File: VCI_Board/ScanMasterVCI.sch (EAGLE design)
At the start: 77 parts, among them IC1 XMEGA16A4A, Q13 MMBT3904, Q14 MMBT3904, Q15 MMBT3904, Q2 NDC7002N, Q3 MMBT3904, Q5 NTZD5110N, Q6 MMBT3904, Q7 ZXMP6A17G, Q8 MMBT4403, Q9 NDC7002N, U1 MAX17502FATB+, U2 SN65HVDA195-Q1, U3 MAX17502EATB+, U4 L78L08ABUTR

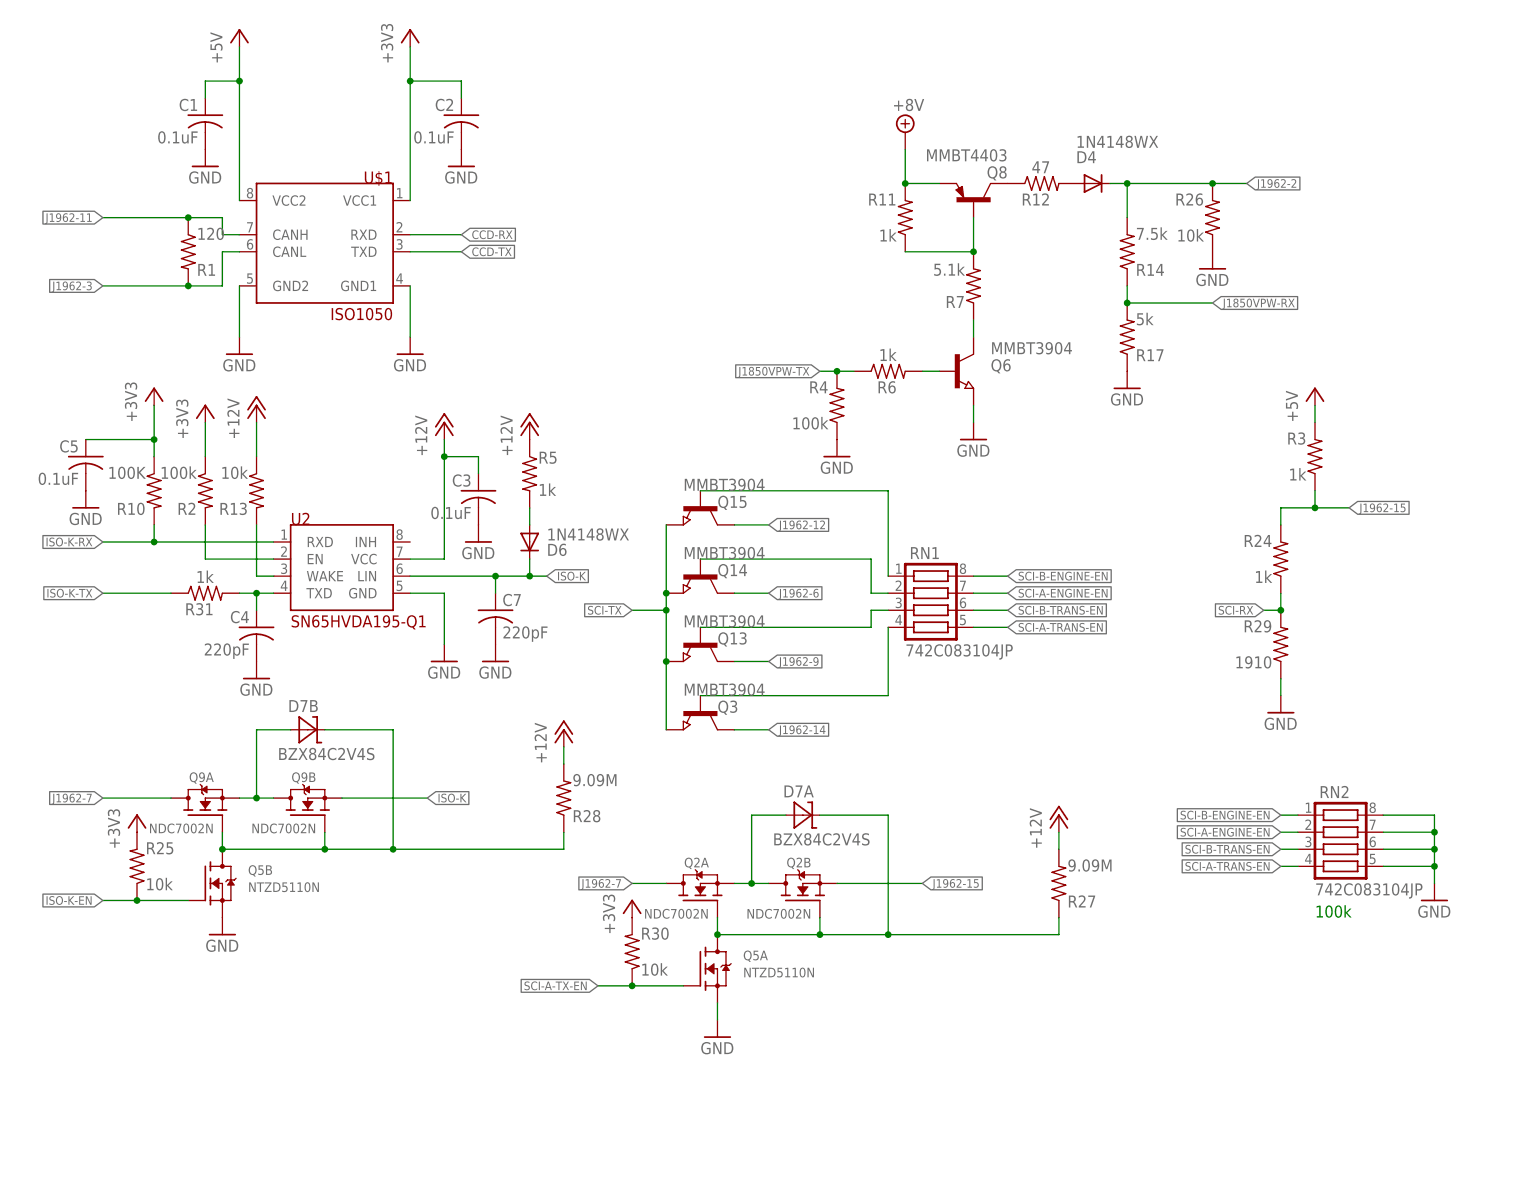
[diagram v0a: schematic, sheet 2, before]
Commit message: It was pointed out to me that the legs of my transistor were reversed. Fixed.
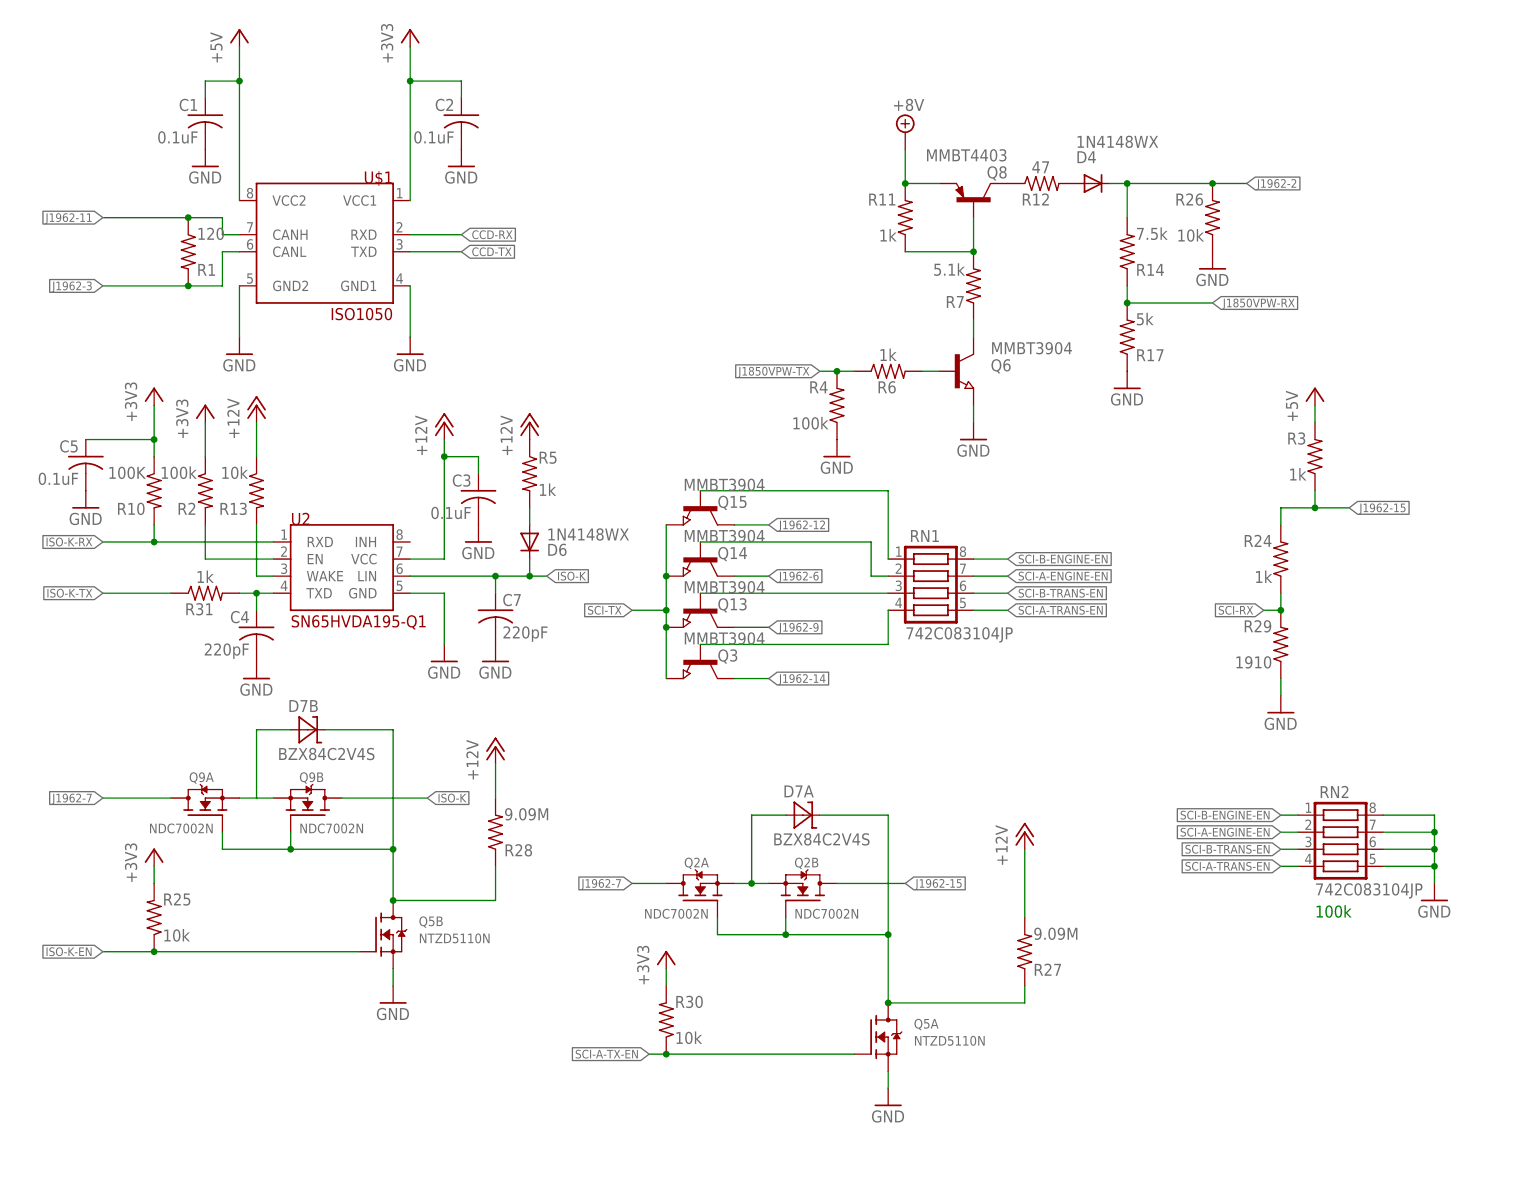
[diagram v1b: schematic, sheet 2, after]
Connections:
- net ISO-K: now also Q9B.D; no longer Q9B.S
- net J1962-15: now also Q2B.D; no longer Q2B.S
- net N$1: now also Q2B.S; no longer Q2B.D
- net N$4: now also Q9B.S; no longer Q9B.D
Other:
- moved on the sheet: Q13, Q14, Q3, Q5A, Q5B, R25, R27, R28, R30, RN1

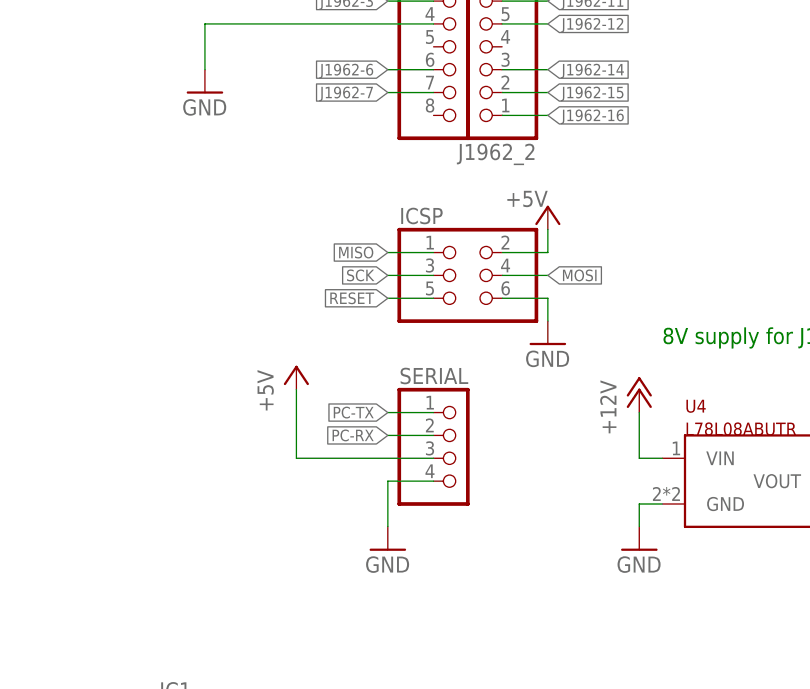
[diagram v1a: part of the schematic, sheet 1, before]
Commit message: Centered the OBD-II "header" pins on the board. Had to move a ton of stuff around to accomodate moving the OBD-II header to the center of the board, but I am now back to auto-router able to 100% route the board.
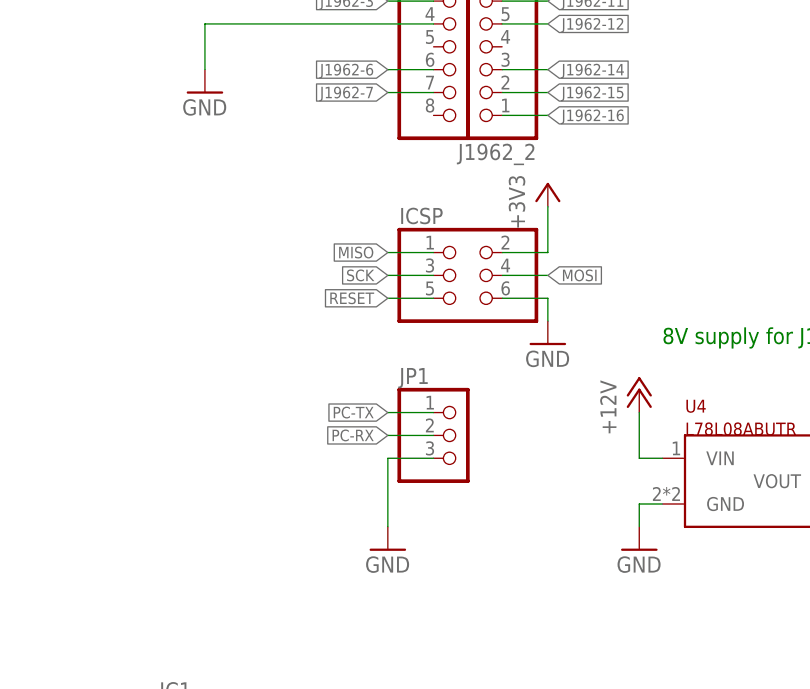
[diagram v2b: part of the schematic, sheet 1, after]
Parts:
- removed SERIAL: (no value), pinhead:PINHD-1X4
- added JP1: (no value), pinhead:PINHD-1X3
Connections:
- net +3V3: now also ICSP.2
- net +5V: no longer ICSP.2, SERIAL.3
- net GND: now also JP1.3; no longer SERIAL.4
- net PC-RX: now also JP1.2; no longer SERIAL.2
- net PC-TX: now also JP1.1; no longer SERIAL.1

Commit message: Started organizing the board. Keeping +12V components next to each other to try and reduce vias. Same for +5v and +3V3. So far not very successful, but it's a WIP.
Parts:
- C1: device adafruit:C-USC0805 -> adafruit:C-USC0603
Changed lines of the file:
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@@
 <grid distance="0.1" unitdist="inch" unit="inch" style="lines" multiple="1" display="no" altdistance="0.01" altunitdist="inch" altunit="inch"/>
 <layers>
-<layer number="1" name="Top" color="4" fill="1" visible="no" active="no"/>
-<layer number="16" name="Bottom" color="1" fill="1" visible="no" active="no"/>
-<layer number="17" name="Pads" color="2" fill="1" visible="no" active="no"/>
-<layer number="18" name="Vias" color="2" fill="1" visible="no" active="no"/>
-<layer number="19" name="Unrouted" color="6" fill="1" visible="no" active="no"/>
-<layer number="20" name="Dimension" color="24" fill="1" visible="no" active="no"/>
-<layer number="21" name="tPlace" color="7" fill="1" visible="no" active="no"/>
-<layer number="22" name="bPlace" color="7" fill="1" visible="no" active="no"/>
-<layer number="23" name="tOrigins" color="15" fill="1" visible="no" active="no"/>
-<layer number="24" name="bOrigins" color="15" fill="1" visible="no" active="no"/>
-<layer number="25" name="tNames" color="7" fill="1" visible="no" active="no"/>
-<layer number="26" name="bNames" color="7" fill="1" visible="no" active="no"/>
-<layer number="27" name="tValues" color="7" fill="1" visible="no" active="no"/>
-<layer number="28" name="bValues" color="7" fill="1" visible="no" active="no"/>
+<layer number="1" name="Top" color="4" fill="1" visible="yes" active="no"/>
+<layer number="16" name="Bottom" color="1" fill="1" visible="yes" active="no"/>
+<layer number="17" name="Pads" color="2" fill="1" visible="yes" active="no"/>
+<layer number="18" name="Vias" color="2" fill="1" visible="yes" active="no"/>
+<layer number="19" name="Unrouted" color="6" fill="1" visible="yes" active="no"/>
+<layer number="20" name="Dimension" color="24" fill="1" visible="yes" active="no"/>
+<layer number="21" name="tPlace" color="7" fill="1" visible="yes" active="no"/>
+<layer number="22" name="bPlace" color="7" fill="1" visible="yes" active="no"/>
+<layer number="23" name="tOrigins" color="15" fill="1" visible="yes" active="no"/>
+<layer number="24" name="bOrigins" color="15" fill="1" visible="yes" active="no"/>
+<layer number="25" name="tNames" color="7" fill="1" visible="yes" active="no"/>
+<layer number="26" name="bNames" color="7" fill="1" visible="yes" active="no"/>
+<layer number="27" name="tValues" color="7" fill="1" visible="yes" active="no"/>
+<layer number="28" name="bValues" color="7" fill="1" visible="yes" active="no"/>
 <layer number="29" name="tStop" color="7" fill="3" visible="no" active="no"/>
 <layer number="30" name="bStop" color="7" fill="6" visible="no" active="no"/>
@@
 <layer number="35" name="tGlue" color="7" fill="4" visible="no" active="no"/>
 <layer number="36" name="bGlue" color="7" fill="5" visible="no" active="no"/>
-<layer number="37" name="tTest" color="7" fill="1" visible="no" active="no"/>
-<layer number="38" name="bTest" color="7" fill="1" visible="no" active="no"/>
+<layer number="37" name="tTest" color="7" fill="1" visible="yes" active="no"/>
+<layer number="38" name="bTest" color="7" fill="1" visible="yes" active="no"/>
 <layer number="39" name="tKeepout" color="4" fill="11" visible="no" active="no"/>
 <layer number="40" name="bKeepout" color="1" fill="11" visible="no" active="no"/>
@@
 <layer number="44" name="Drills" color="7" fill="1" visible="no" active="no"/>
 <layer number="45" name="Holes" color="7" fill="1" visible="no" active="no"/>
-<layer number="46" name="Milling" color="3" fill="1" visible="no" active="no"/>
-<layer number="47" name="Measures" color="7" fill="1" visible="no" active="no"/>
-<layer number="48" name="Document" color="7" fill="1" visible="no" active="no"/>
-<layer number="49" name="Reference" color="7" fill="1" visible="no" active="no"/>
-<layer number="50" name="dxf" color="7" fill="1" visible="no" active="no"/>
-<layer number="51" name="tDocu" color="7" fill="1" visible="no" active="no"/>
-<layer number="52" name="bDocu" color="7" fill="1" visible="no" active="no"/>
-<layer number="53" name="tGND_GNDA" color="7" fill="9" visible="no" active="no"/>
-<layer number="54" name="bGND_GNDA" color="1" fill="9" visible="no" active="no"/>
-<layer number="56" name="wert" color="7" fill="1" visible="no" active="no"/>
-<layer number="57" name="tCAD" color="7" fill="1" visible="no" active="no"/>
-<layer number="59" name="tCarbon" color="7" fill="1" visible="no" active="no"/>
-<layer number="60" name="bCarbon" color="7" fill="1" visible="no" active="no"/>
-<layer number="61" name="stand" color="7" fill="1" visible="no" active="no"/>
+<layer number="46" name="Milling" color="3" fill="1" visible="yes" active="no"/>
+<layer number="47" name="Measures" color="7" fill="1" visible="yes" active="no"/>
+<layer number="48" name="Document" color="7" fill="1" visible="yes" active="no"/>
+<layer number="49" name="Reference" color="7" fill="1" visible="yes" active="no"/>
+<layer number="50" name="dxf" color="7" fill="1" visible="yes" active="no"/>
+<layer number="51" name="tDocu" color="7" fill="1" visible="yes" active="no"/>
+<layer number="52" name="bDocu" color="7" fill="1" visible="yes" active="no"/>
+<layer number="53" name="tGND_GNDA" color="7" fill="9" visible="yes" active="no"/>
+<layer number="54" name="bGND_GNDA" color="1" fill="9" visible="yes" active="no"/>
+<layer number="56" name="wert" color="7" fill="1" visible="yes" active="no"/>
+<layer number="57" name="tCAD" color="7" fill="1" visible="yes" active="no"/>
+<layer number="59" name="tCarbon" color="7" fill="1" visible="yes" active="no"/>
+<layer number="60" name="bCarbon" color="7" fill="1" visible="yes" active="no"/>
+<layer number="61" name="stand" color="7" fill="1" visible="yes" active="no"/>
 <layer number="88" name="SimResults" color="9" fill="1" visible="yes" active="yes"/>
 <layer number="89" name="SimProbes" color="9" fill="1" visible="yes" active="yes"/>
@@
 <part name="GND8" library="supply1" library_urn="urn:adsk.eagle:library:371" deviceset="GND" device=""/>
 <part name="GND10" library="supply1" library_urn="urn:adsk.eagle:library:371" deviceset="GND" device=""/>
-<part name="C1" library="adafruit" library_urn="urn:adsk.eagle:library:420" deviceset="C-US" device="C0805" value="0.1uF"/>
+<part name="C1" library="adafruit" library_urn="urn:adsk.eagle:library:420" deviceset="C-US" device="C0603" value="0.1uF"/>
 <part name="GND5" library="supply1" library_urn="urn:adsk.eagle:library:371" deviceset="GND" device=""/>
 <part name="C2" library="adafruit" library_urn="urn:adsk.eagle:library:420" deviceset="C-US" device="C0603" value="0.1uF"/>
